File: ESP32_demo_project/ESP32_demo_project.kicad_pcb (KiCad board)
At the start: 4 copper layers, 118 x 58 mm, 87 parts, among them J1 SS-52400-002, J2 B2B-PH-SM4-TB, J3 GSD090012SEU, J4 Conn_01x04_Pin, J5 Conn_01x05_Pin, Q1 TEMT6000X01, Q2 BC817, Q3 BC817, U1 MCP73871, U2 BME280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

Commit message: main: updating layout with lock
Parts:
- moved TP5 44.6 mm to (211.8, 108.5)
- moved TP1 44.2 mm to (211.2, 94.8)
- moved TP3 44.2 mm to (211.2, 100.9)
- moved TP4 44.2 mm to (211.2, 104.0)
- moved C9 19.9 mm to (129.9, 100.5)
- moved C12 15.8 mm to (187.8, 94.2)
- moved TP2 15.7 mm to (179.0, 92.0)
- moved C16 9.69 mm to (134.3, 74.7)
- moved C17 9.69 mm to (134.3, 77.7)
- moved C18 9.69 mm to (134.3, 80.7)
- moved R28 9.69 mm to (125.5, 83.5)
- moved U7 9.69 mm to (124.1, 77.3)
- moved R29 9.69 mm to (129.9, 71.7)
- moved R30 9.69 mm to (129.9, 74.6)
- moved R31 9.69 mm to (129.9, 77.5)
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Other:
- board size 118 x 58 mm -> 112 x 58.5 mm

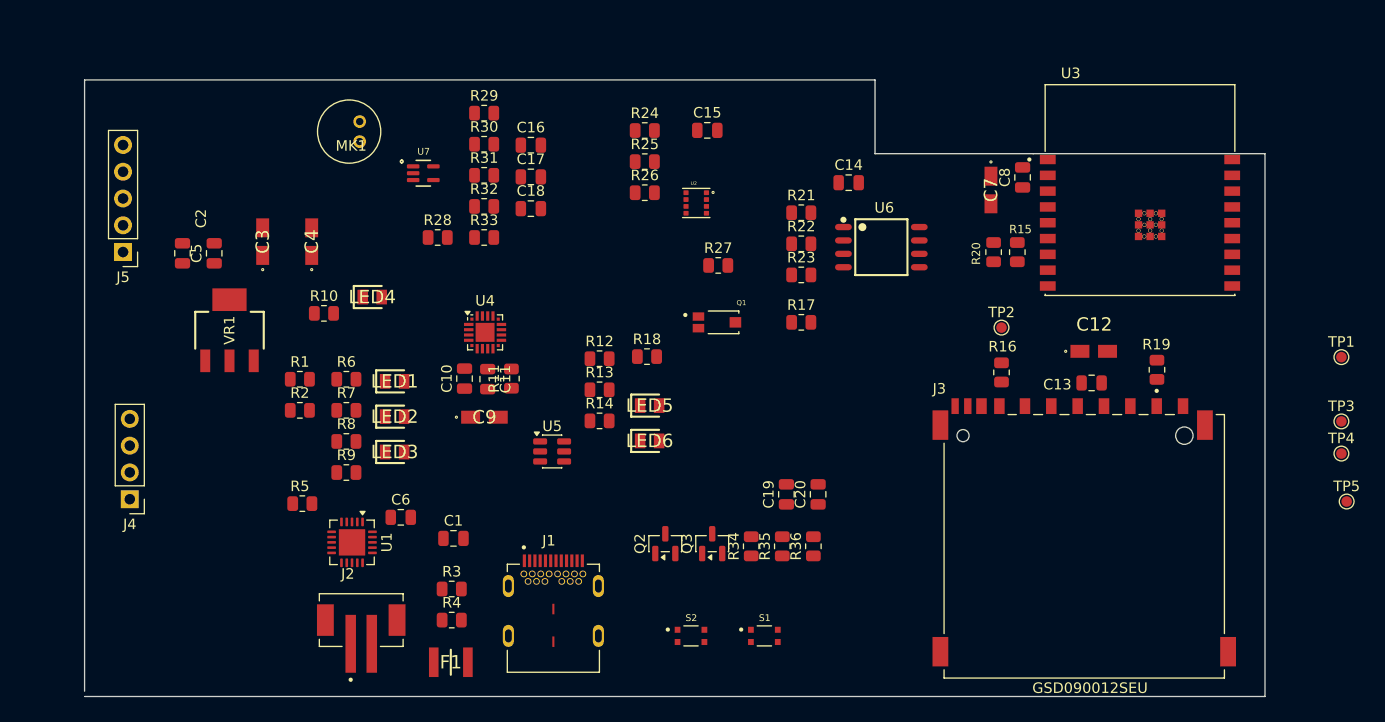
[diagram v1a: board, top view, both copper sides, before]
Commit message: main: updated placement
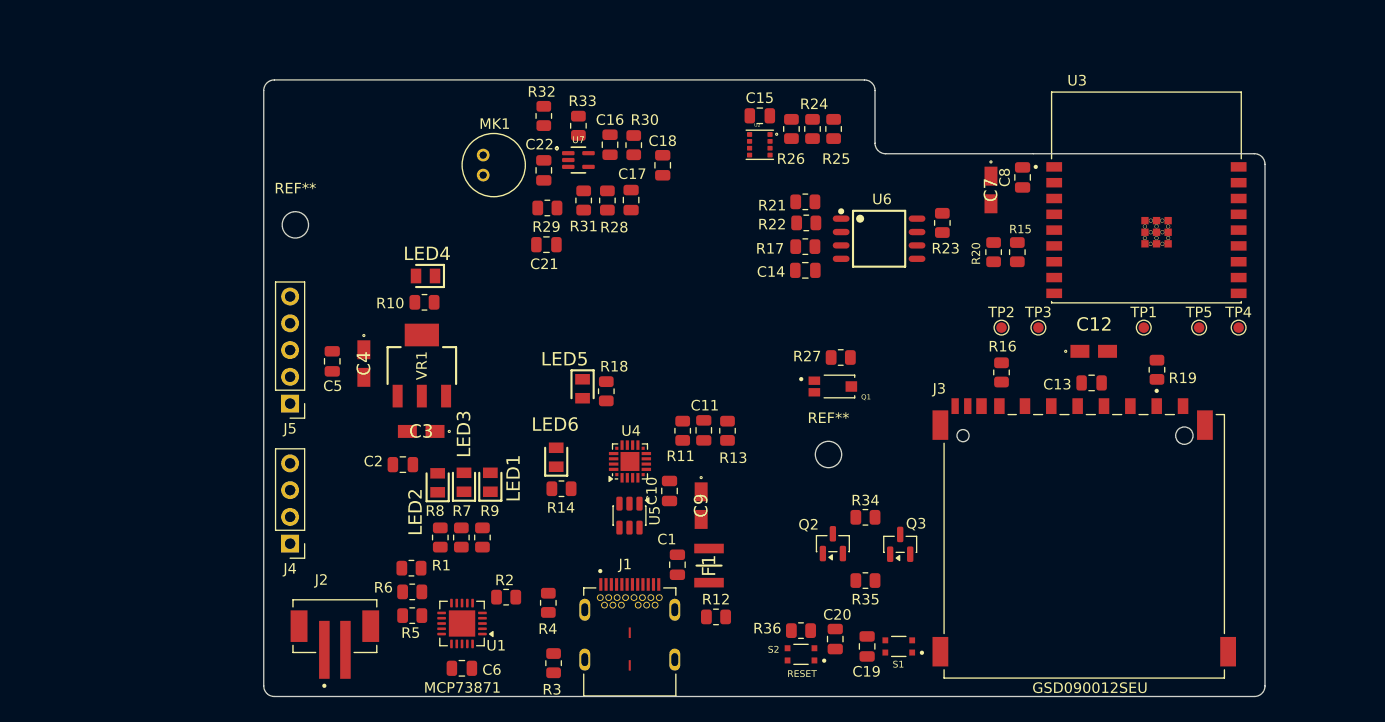
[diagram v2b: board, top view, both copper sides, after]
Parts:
- added C21: 1u, Capacitor_SMD:C_0805_2012Metric, F.Cu at (135.8, 84.1)
- added C22: 1n, Capacitor_SMD:C_0805_2012Metric, F.Cu at (135.6, 77.1)
- added REF**: MountingHole_2.5mm, MountingHole:MountingHole_2.5mm, F.Cu at (112.0, 82.2)
- added REF**: MountingHole_2.5mm, MountingHole:MountingHole_2.5mm, F.Cu at (162.6, 104.0)
- moved TP3 30.1 mm to (182.5, 92.0)
- moved C2 29.0 mm to (122.2, 105.0), turned to 180 degrees
- moved R12 26.9 mm to (151.9, 119.5)
- moved R2 26.4 mm to (132.0, 117.6)
- moved F1 26.2 mm to (151.2, 114.6), turned to 90 degrees
- moved C3 23.5 mm to (123.9, 101.8), turned to 180 degrees
- moved C9 22.2 mm to (150.5, 108.9), turned to -90 degrees
- moved C10 22.2 mm to (147.5, 107.5)
- moved TP5 21.6 mm to (197.8, 92.0)
- moved J5 21.4 mm to (111.5, 99.2)
- moved C1 21.4 mm to (148.2, 114.5), turned to 90 degrees
- moved R6 21.1 mm to (123.1, 117.1)
- moved C11 21.1 mm to (150.8, 101.8), turned to 90 degrees
- moved R1 20.8 mm to (123.0, 114.8), turned to 180 degrees
- moved TP1 19.0 mm to (192.5, 92.0)
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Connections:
- C18 pad 2: GND -> Net-(C18-Pad2)
- MK1 pad GND: GND -> Net-(C18-Pad2)
- MK1 pad OUT: Net-(U7-IN+) -> Net-(C22-Pad2)
- R29 pad 1: GND -> Net-(C21-Pad1)
- R31 pad 1: GND -> Net-(C18-Pad2)
- R32 pad 1: Net-(U7-IN+) -> Net-(C22-Pad2)
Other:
- board size 112 x 58.5 mm -> 95 x 58.5 mm

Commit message: main: added copper zones
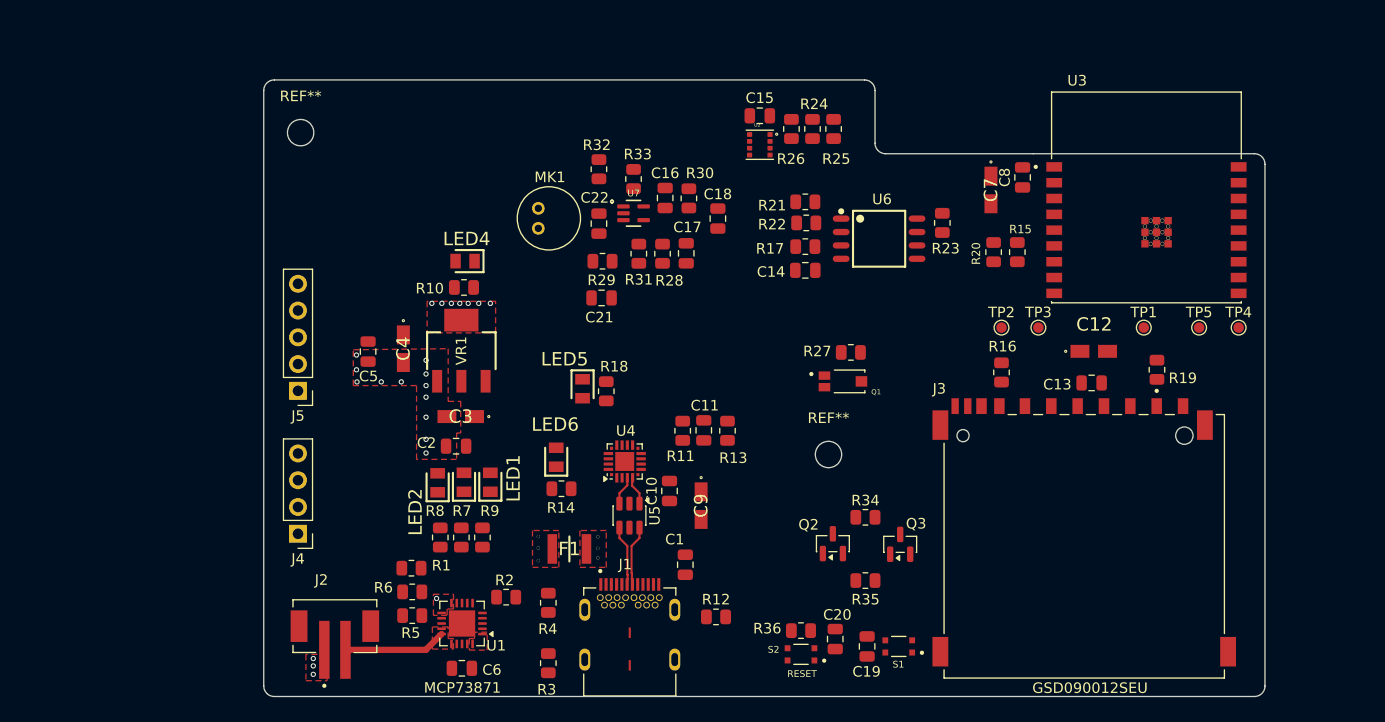
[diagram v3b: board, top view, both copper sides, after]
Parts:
- moved F1 13.3 mm to (138.0, 113.0), turned to 180 degrees
- moved REF** 8.76 mm to (112.5, 73.5)
- moved C16 7.27 mm to (147.1, 79.7)
- moved C17 7.27 mm to (149.1, 85.0)
- moved C21 7.27 mm to (141.1, 89.2)
- moved C22 7.27 mm to (140.8, 82.1)
- moved MK1 7.27 mm to (136.1, 81.6)
- moved R28 7.27 mm to (146.8, 85.0)
- moved R30 7.27 mm to (149.3, 79.7)
- moved R31 7.27 mm to (144.6, 85.0)
- moved R32 7.27 mm to (140.8, 77.0)
- moved C18 7.27 mm to (152.1, 81.7)
- moved R33 7.27 mm to (144.1, 77.9)
- moved U7 7.27 mm to (144.1, 81.2)
- moved R29 7.27 mm to (141.1, 85.7)
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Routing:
- net /VBAT: track 0.00 -> 9.75 mm
- net /USB_DP: track 0.00 -> 5.74 mm
- net /USB_DN: track 0.00 -> 5.74 mm
- net /ESP32-C3-02/USB_D+: track 0.00 -> 2.76 mm
- net /ESP32-C3-02/USB_D-: track 0.00 -> 2.76 mm
- net GND: vias 0 -> 16
- net /VBUS: vias 0 -> 3
- net /+5V_VBUS: vias 0 -> 3
- net +3.3V: vias 0 -> 7
- added copper zone on F.Cu, net +3.3V
- added copper zone on In1.Cu, net +3.3V
- added copper zone on F.Cu, net +5V
- added copper zone on F.Cu, net /+5V_VBUS
- added copper zone on In1.Cu, net /+5V_VBUS
- added copper zone on F.Cu, net /VBAT
- added copper zone on F.Cu, net /VBUS
- added copper zone on In1.Cu, net /VBUS
- added copper zone on F.Cu, net GND
- added copper zone on In2.Cu, net GND
